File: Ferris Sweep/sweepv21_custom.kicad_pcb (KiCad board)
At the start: 2 copper layers, 217.4 x 86.9 mm, 48 parts, among them J1 AudioJack4dpb, J2 AudioJack4dpb, SW10 SW_Push, SW11 SW_Push, SW11_r1 SW_Push, SW12 SW_Push, SW12_r1 SW_Push, SW13_r1 SW_Push, SW14 SW_Push, SW15 SW_Push, SW15_r1 SW_Push, SW16 SW_Push, SW16_r1 SW_Push, SW17 SW_Push, SW17_r1 SW_Push, SW18 SW_Push, SW18_r1 SW_Push, SW2 SW_Push, SW20 SW_Push, SW20_r1 SW_Push, SW21 SW_Push, SW21_r1 SW_Push, SW2_r1 SW_Push, SW3 SW_Push, SW3_r1 SW_Push, SW4 SW_Push, SW4_r1 SW_Push, SW5 SW_Push, SW5_r1 SW_Push, SW6 SW_Push, SW6_r1 SW_Push, SW7_r1 SW_Push, SW8 SW_Push, SW8_r1 SW_Push, SW9 SW_Push, SW9_r1 SW_Push, U1 ProMicro-kbd, U2 ProMicro-kbd

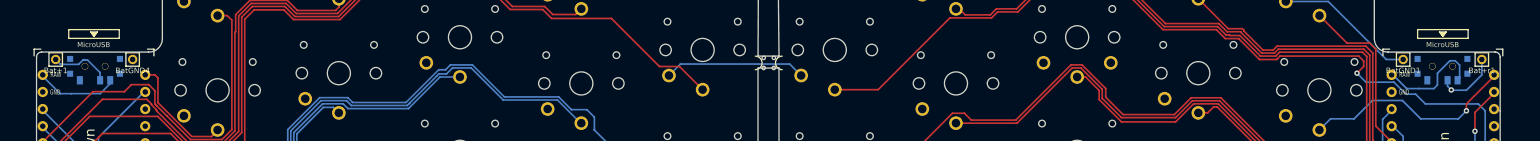
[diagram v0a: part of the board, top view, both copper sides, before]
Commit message: Update silkscreen, add image
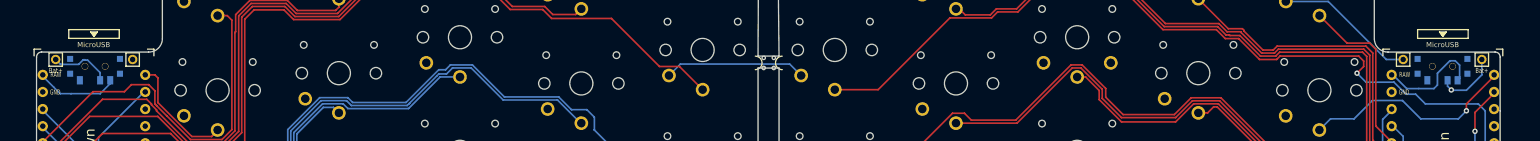
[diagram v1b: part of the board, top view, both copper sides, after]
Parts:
-  : renamed from BatGND4
-  : renamed from BatGND1
- renumbered Bat+r1 to Bat+, Bat+1 to Bat+, SW_POWERR1 to SW, SW_POWER1 to SW

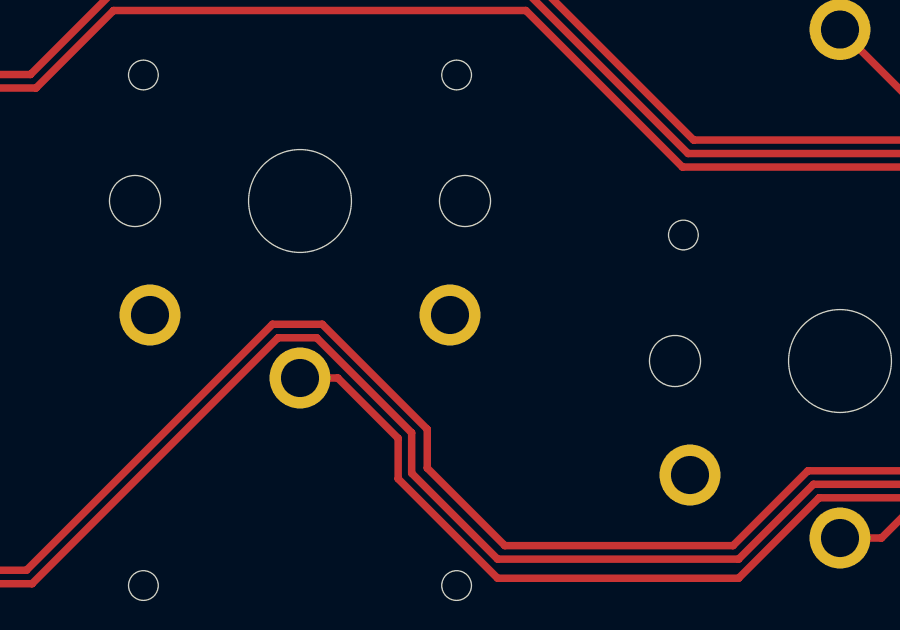
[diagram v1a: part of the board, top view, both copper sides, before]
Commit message: Minor trace changes
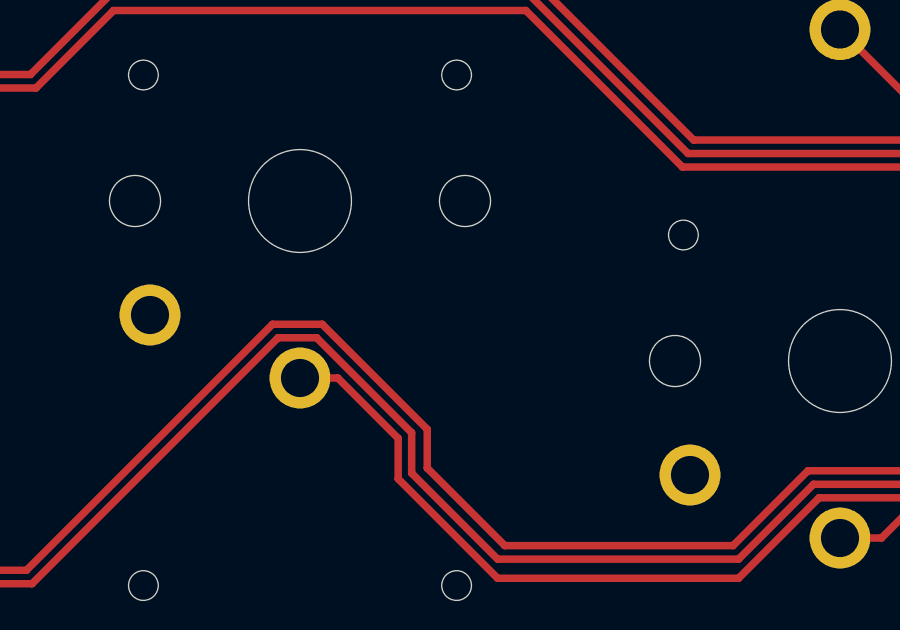
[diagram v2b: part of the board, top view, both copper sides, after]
